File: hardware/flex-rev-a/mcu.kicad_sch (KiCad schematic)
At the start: 1 part, among them U1 ISP2454-LX

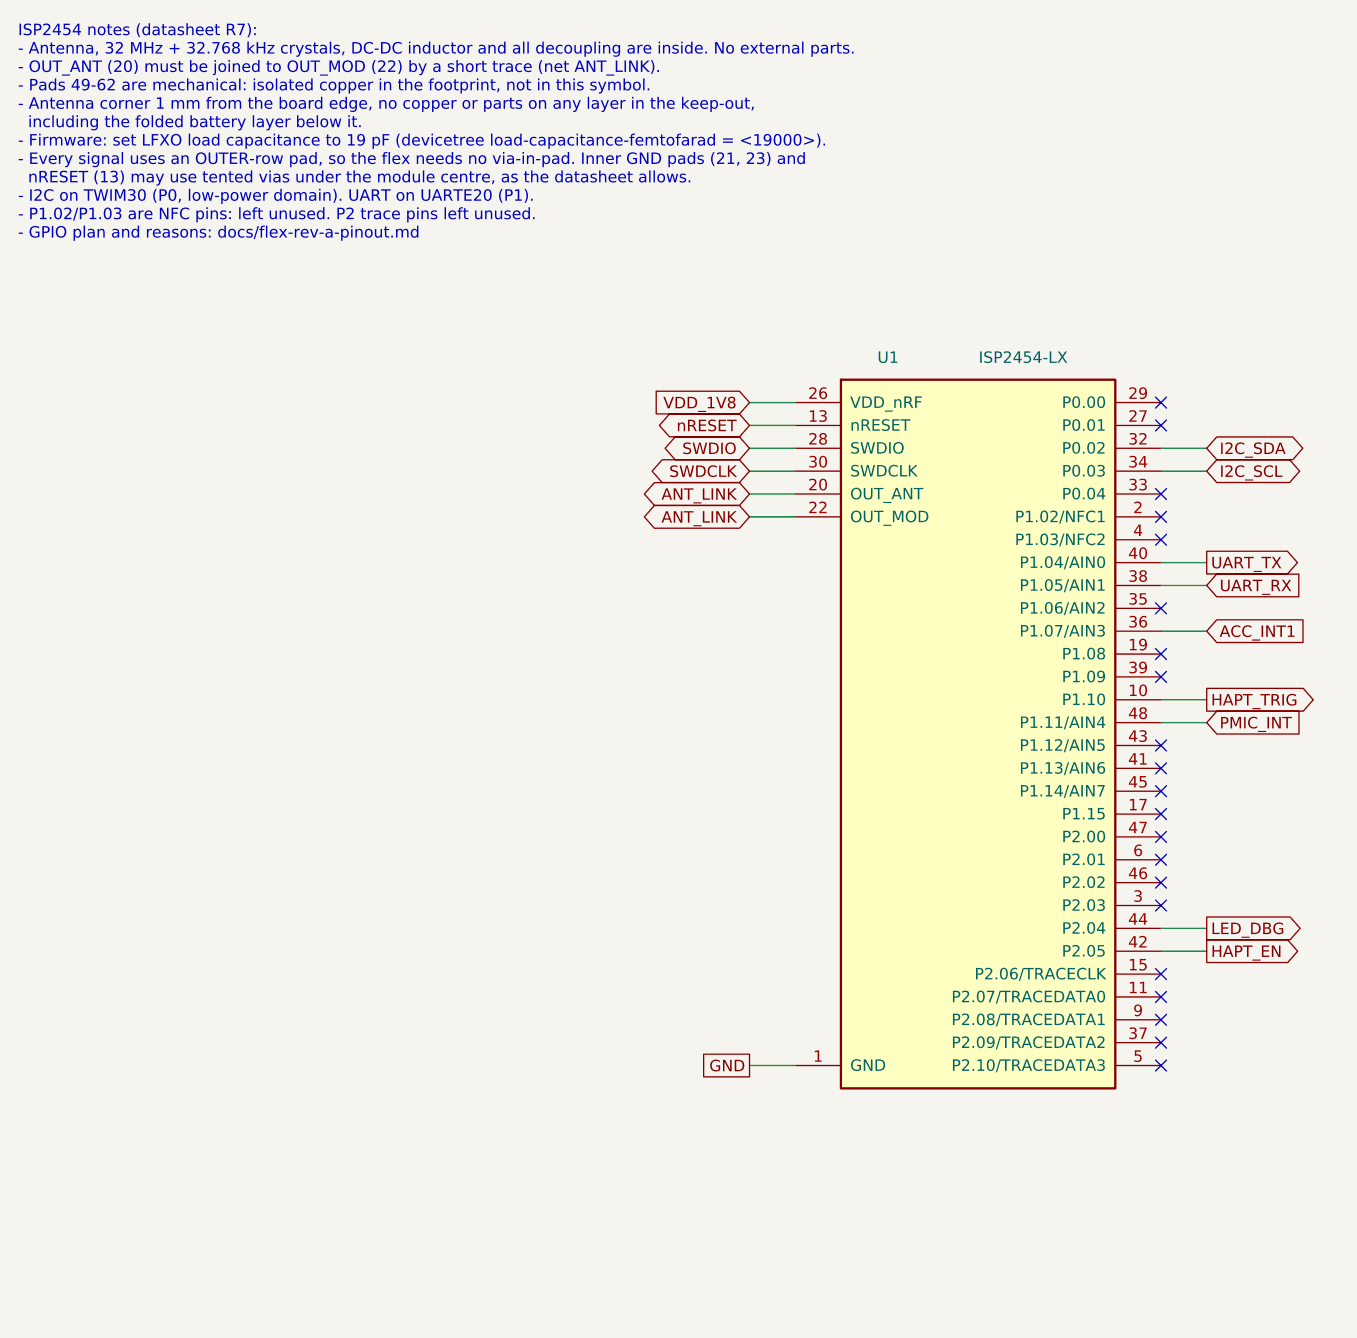
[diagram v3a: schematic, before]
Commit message: Apply schematic review fixes: 2.0 V rail, pad 10 NC, VIN TVS, bulk cap
- Power: R202 47k -> 68k so BUCK1 starts at 2.0 V; global net VDD_1V8
  renamed VDD_2V0 on every sheet, notes updated.
- Haptics: DRV2605L IN/TRIG tied to GND, HAPT_TRIG removed (effects run
  over I2C). Footprint kept as Package_SO:TSSOP-10_3x3mm_P0.5mm: it is
  KiCad's TI DGS land pattern (cites MPDS035); KiCad 10 has no footprint
  named VSSOP-10_3x3mm_P0.5mm.
- MCU: pad 10 (P1.10) no-connect; GND global label replaced by the GND
  power symbol; note on the trapped lower-row GND pads 12/14/16/18 and on
  pads 8/24.
- Sensors: C403 10 uF on LIS2DW12 VDD per ST; related (check) removed.
- Dock: VIN TVS is now Littelfuse SMF18A (SOD-123FL, 18 V standoff, LCSC
  C409420); data pads keep TPD1E10B06, TPD1E0B04 noted as a lower-leakage
  alternative (check).
- bom.csv regenerated, PDF replotted, README updated.

ERC: 0 errors, 0 warnings.

Co-Authored-By: Claude Opus 5.5 <noreply@anthropic.com>
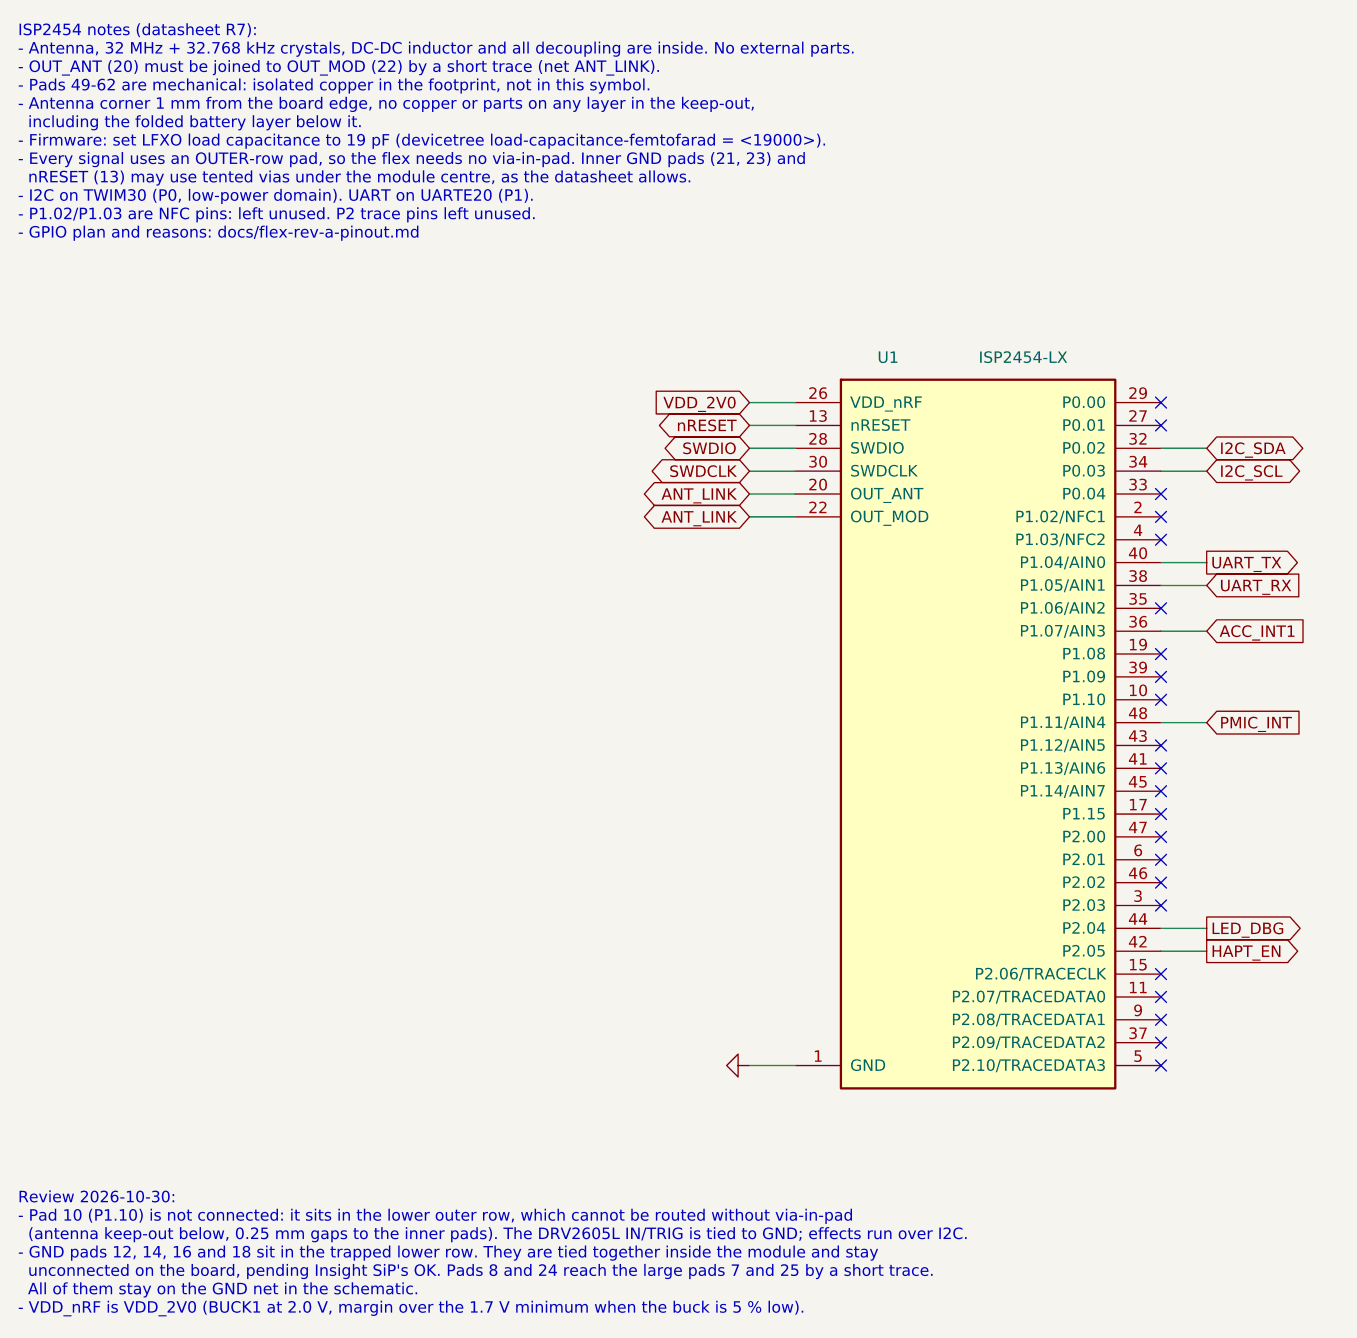
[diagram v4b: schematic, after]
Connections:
- net HAPT_TRIG: no longer names the net of U1.10 (P1.10)
- net VDD_1V8 renamed VDD_2V0
- no-connect marks 21 -> 22
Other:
- note added: "Review 2026-10-30: - Pad 10 (P1.10) is not connected: it sits in the lower outer row, which cannot be routed without via-in-pad (antenna keep-out below, 0.25 mm gaps to the inner pads). The DRV2605L IN/TRIG is tied to GND; effects run over I2C. - GND pads 12, 14, 16 and 18 sit in the trapped lower row. They are tied together inside the module and stay unconnected on the board, pending Insight SiP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"
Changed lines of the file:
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@@
 		(comment 1 "Plan: docs/flex-pcb-schematic-plan.md")
+	)
+	(text "Review 2026-10-30:\n- Pad 10 (P1.10) is not connected: it sits in the lower outer row, which cannot be routed without via-in-pad\n  (antenna keep-out below, 0.25 mm gaps to the inner pads). The DRV2605L IN/TRIG is tied to GND; effects run over I2C.\n- GND pads 12, 14, 16 and 18 sit in the trapped lower row. They are tied together inside the module and stay\n  unconnected on the board, pending Insight SiP's OK. Pads 8 and 24 reach the large pads 7 and 25 by a short trace.\n  All of them stay on the GND net in the schematic.\n- VDD_nRF is VDD_2V0 (BUCK1 at 2.0 V, margin over the 1.7 V minimum when the buck is 5 % low)."
+		(exclude_from_sim no)
+		(at 20.32 150 0)
+		(effects
+			(font
+				(size 1.27 1.27)
+			)
+			(justify left top)
+		)
 	)
 	(text "ISP2454 notes (datasheet R7):\n- Antenna, 32 MHz + 32.768 kHz crystals, DC-DC inductor and all decoupling are inside. No external parts.\n- OUT_ANT (20) must be joined to OUT_MOD (22) by a short trace (net ANT_LINK).\n- Pads 49-62 are mechanical: isolated copper in the footprint, not in this symbol.\n- Antenna corner 1 mm from the board edge, no copper or parts on any layer in the keep-out,\n  including the folded battery layer below it.\n- Firmware: set LFXO load capacitance to 19 pF (devicetree load-capacitance-femtofarad = <19000>).\n- Every signal uses an OUTER-row pad, so the flex needs no via-in-pad. Inner GND pads (21, 23) and\n  nRESET (13) may use tented vias under the module centre, as the datasheet allows.\n- I2C on TWIM30 (P0, low-power domain). UART on UARTE20 (P1).\n- P1.02/P1.03 are NFC pins: left unused. P2 trace pins left unused.\n- GPIO plan and reasons: docs/flex-rev-a-pinout.md"
@@
 	)
 	(no_connect
+		(at 147.32 95.25)
+	)
+	(no_connect
 		(at 147.32 113.03)
 	)
@@
 		(pts
 			(xy 147.32 123.19) (xy 152.4 123.19)
-		)
-		(stroke
-			(width 0)
-			(type default)
-		)
-	)
-	(wire
-		(pts
-			(xy 147.32 95.25) (xy 152.4 95.25)
 		)
 		(stroke
@@
 		)
 	)
-	(global_label "VDD_1V8"
+	(global_label "VDD_2V0"
 		(shape input)
 		(at 101.6 62.23 180)
@@
 			)
 			(justify right)
-		)
-		(property "Intersheetrefs" "${INTERSHEET_REFS}"
-			(at 0 0 0)
-			(hide yes)
-			(show_name no)
-			(do_not_autoplace no)
-			(effects
-				(font
-					(size 1.27 1.27)
-				)
-			)
-		)
-	)
-	(global_label "HAPT_TRIG"
-		(shape output)
-		(at 152.4 95.25 0)
-		(fields_autoplaced yes)
-		(effects
-			(font
-				(size 1.27 1.27)
-			)
-			(justify left)
 		)
 		(property "Intersheetrefs" "${INTERSHEET_REFS}"
@@
 			)
 			(justify left)
-		)
-		(property "Intersheetrefs" "${INTERSHEET_REFS}"
-			(at 0 0 0)
-			(hide yes)
-			(show_name no)
-			(do_not_autoplace no)
-			(effects
-				(font
-					(size 1.27 1.27)
-				)
-			)
-		)
-	)
-	(global_label "GND"
-		(shape passive)
-		(at 101.6 135.89 180)
-		(fields_autoplaced yes)
-		(effects
-			(font
-				(size 1.27 1.27)
-			)
-			(justify right)
 		)
 		(property "Intersheetrefs" "${INTERSHEET_REFS}"
@@
 					(unit 1)
 				)
+			)
+		)
+	)
+	(symbol
+		(lib_id "power:GND")
+		(at 101.6 135.89 270)
+		(unit 1)
+		(body_style 1)
+		(exclude_from_sim no)
+		(in_bom yes)
+		(on_board yes)
+		(in_pos_files yes)
+		(dnp no)
+		(property "Reference" "#PWR301"
+			(at 101.6 135.89 0)
+			(hide yes)
+			(show_name no)
+			(do_not_autoplace no)
+			(effects
+				(font
+					(size 1.27 1.27)
+				)
+			)
+		)
+		(property "Value" "GND"
+			(at 101.6 139.7 0)
+			(hide yes)
+			(show_name no)
+			(do_not_autoplace no)
+			(effects
+				(font
+					(size 1.27 1.27)
+				)
+			)
+		)
+		(property "Footprint" ""
+			(at 101.6 135.89 0)
+			(hide yes)
+			(show_name no)
+			(do_not_autoplace no)
+			(effects
+				(font
+					(size 1.27 1.27)
+				)
+			)
+		)
+		(property "Datasheet" ""
+			(at 101.6 135.89 0)
+			(hide yes)
+			(show_name no)
+			(do_not_autoplace no)
+			(effects
+				(font
+					(size 1.27 1.27)
+				)
+			)
+		)
+		(property "Description" ""
+			(at 101.6 135.89 0)
+			(show_name no)
+			(do_not_autoplace no)
+			(effects
+				(font
+					(size 1.27 1.27)
+				)
+			)
+		)
+		(pin "1"
+		)
+		(instances
+			(project "flex-rev-a"
+				(path "/f1a047c3-8922-464f-af19-ac9fc5db330b/17001d3b-fbd8-4f96-b500-59fa238486df"
+					(reference "#PWR301")
+					(unit 1)
+				)
